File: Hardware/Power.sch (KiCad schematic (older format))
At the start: 20 parts

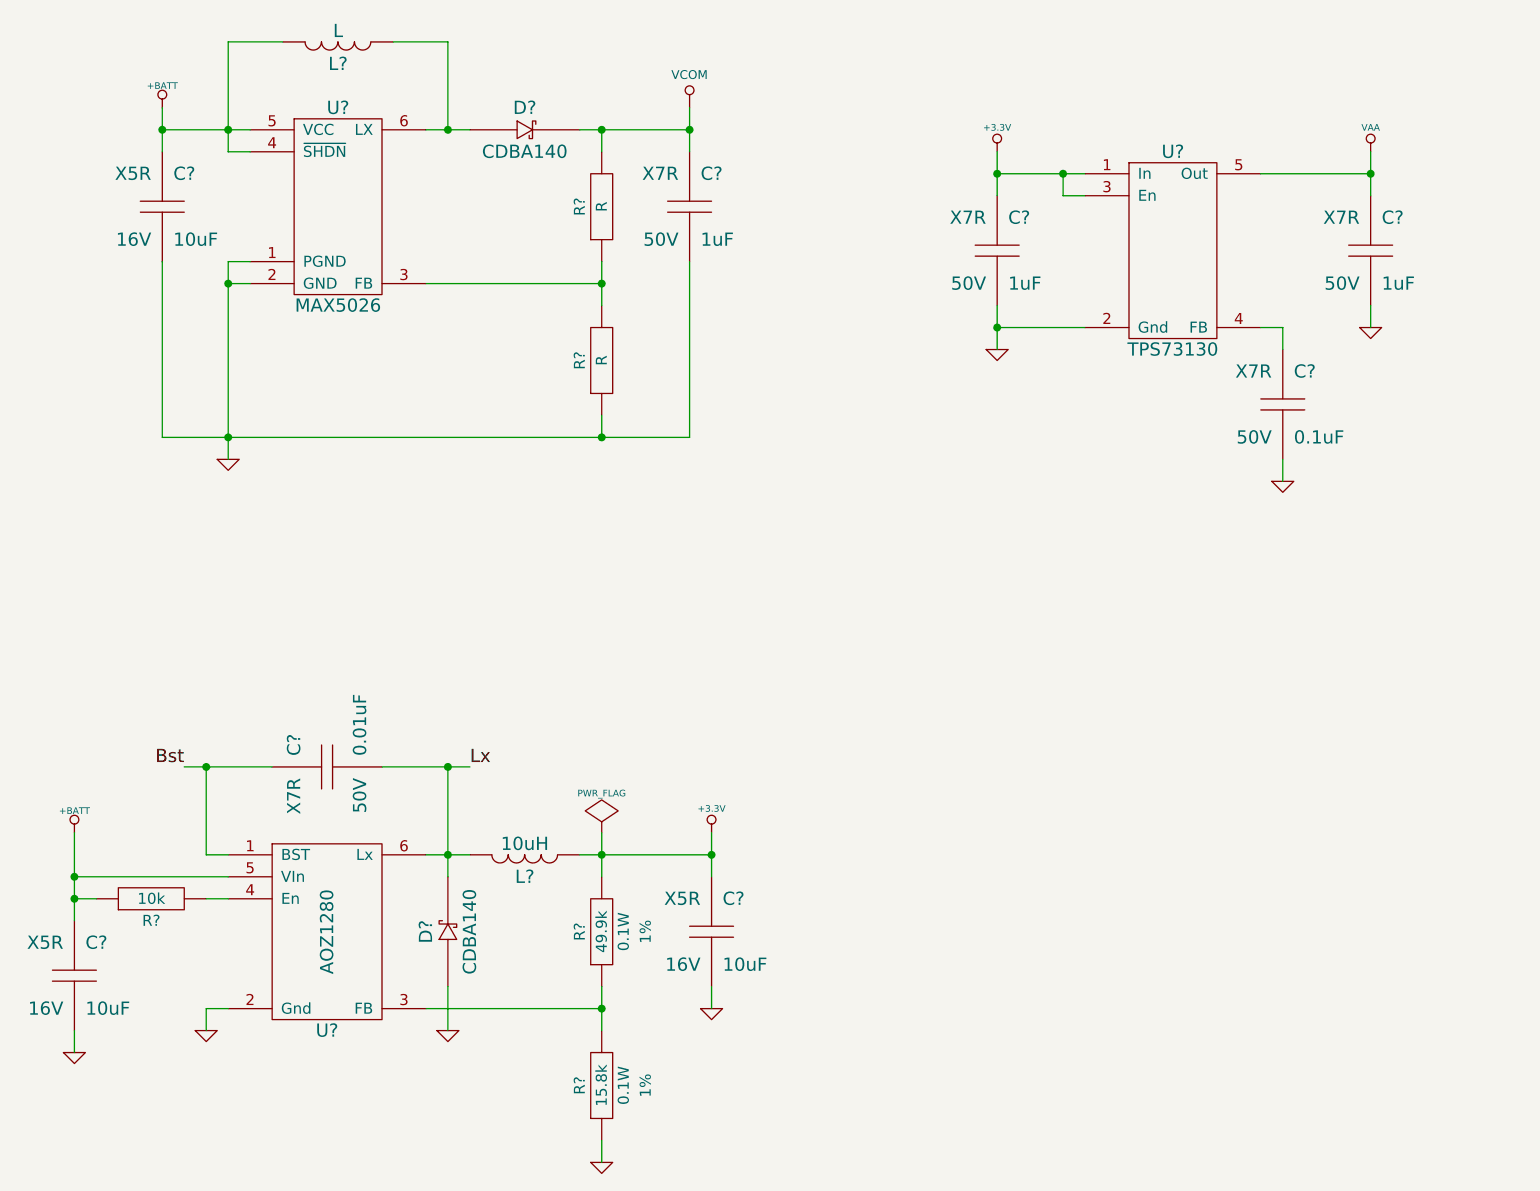
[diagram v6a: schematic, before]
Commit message: Rough layout for pin map testing
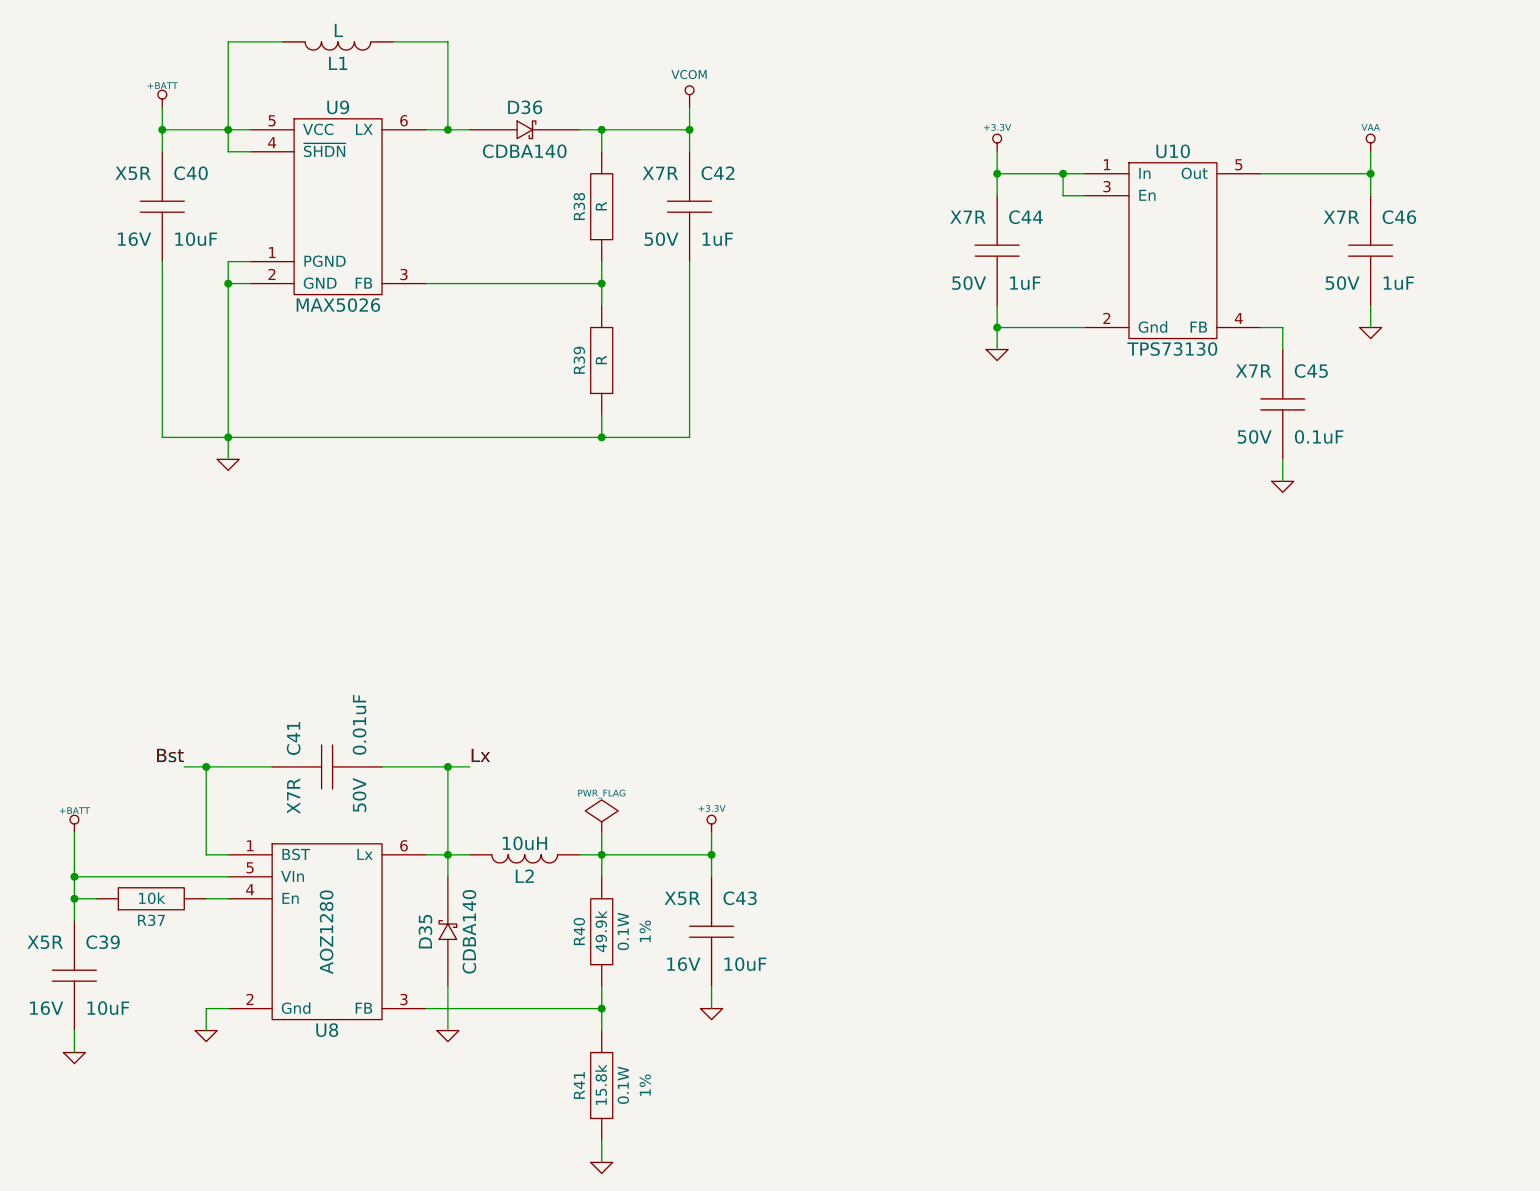
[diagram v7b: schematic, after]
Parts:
- gave numbers to parts that had none: 20
